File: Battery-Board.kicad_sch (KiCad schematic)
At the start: 0 parts

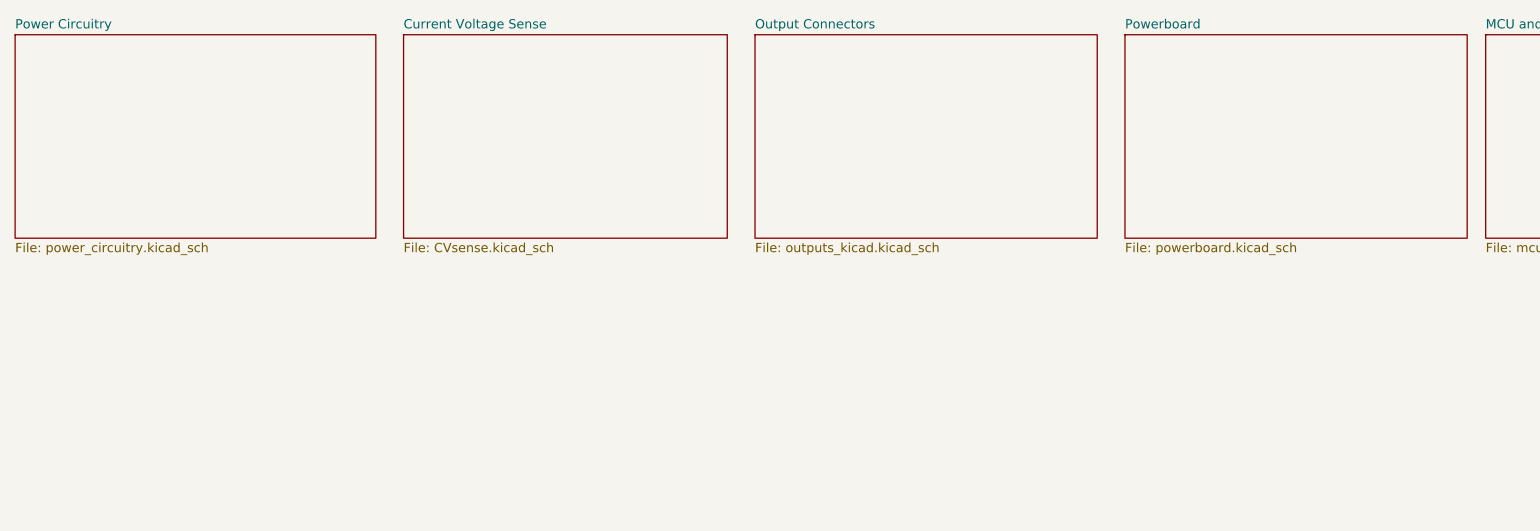
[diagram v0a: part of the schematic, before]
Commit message: started sorting and cleaning up schemativc
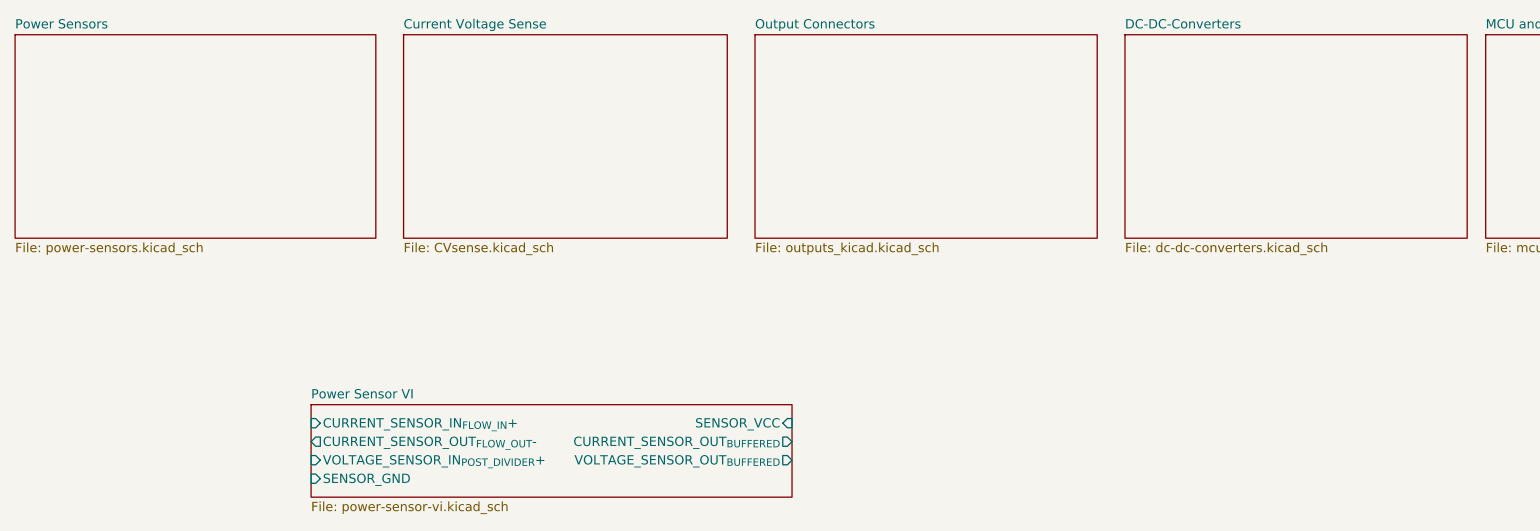
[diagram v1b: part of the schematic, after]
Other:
- sheet Power Circuitry renamed Power Sensors
- sheet Powerboard renamed DC-DC-Converters
- added sheet Power Sensor VI (power-sensor-vi.kicad_sch)
- sheet DC-DC-Converters: file powerboard.kicad_sch -> dc-dc-converters.kicad_sch
- sheet Power Sensors: file power_circuitry.kicad_sch -> power-sensors.kicad_sch
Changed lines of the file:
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@@
 			(color 0 0 0 0.0000)
 		)
-		(property "Sheetname" "Powerboard"
+		(property "Sheetname" "DC-DC-Converters"
 			(at 167.64 14.5284 0)
 			(effects
@@
 			)
 		)
-		(property "Sheetfile" "powerboard.kicad_sch"
+		(property "Sheetfile" "dc-dc-converters.kicad_sch"
 			(at 167.64 43.7646 0)
 			(effects
@@
 	)
 	(sheet
+		(at 55.88 66.04)
+		(size 66.04 12.7)
+		(fields_autoplaced yes)
+		(stroke
+			(width 0.1524)
+			(type solid)
+		)
+		(fill
+			(color 255 255 194 1.0000)
+		)
+		(property "Sheetname" "Power Sensor VI"
+			(at 55.88 65.3284 0)
+			(effects
+				(font
+					(size 1.27 1.27)
+				)
+				(justify left bottom)
+			)
+		)
+		(property "Sheetfile" "power-sensor-vi.kicad_sch"
+			(at 55.88 79.3246 0)
+			(effects
+				(font
+					(size 1.27 1.27)
+				)
+				(justify left top)
+			)
+		)
+		(pin "CURRENT_SENSOR_IN_{FLOW_IN}+" input
+			(at 55.88 68.58 180)
+			(effects
+				(font
+					(size 1.27 1.27)
+				)
+				(justify left)
+			)
+		)
+		(pin "SENSOR_VCC" input
+			(at 121.92 68.58 0)
+			(effects
+				(font
+					(size 1.27 1.27)
+				)
+				(justify right)
+			)
+		)
+		(pin "CURRENT_SENSOR_OUT_{FLOW_OUT}-" output
+			(at 55.88 71.12 180)
+			(effects
+				(font
+					(size 1.27 1.27)
+				)
+				(justify left)
+			)
+		)
+		(pin "CURRENT_SENSOR_OUT_{BUFFERED}" output
+			(at 121.92 71.12 0)
+			(effects
+				(font
+					(size 1.27 1.27)
+				)
+				(justify right)
+			)
+		)
+		(pin "SENSOR_GND" input
+			(at 55.88 76.2 180)
+			(effects
+				(font
+					(size 1.27 1.27)
+				)
+				(justify left)
+			)
+		)
+		(pin "VOLTAGE_SENSOR_IN_{POST_DIVIDER}+" input
+			(at 55.88 73.66 180)
+			(effects
+				(font
+					(size 1.27 1.27)
+				)
+				(justify left)
+			)
+		)
+		(pin "VOLTAGE_SENSOR_OUT_{BUFFERED}" output
+			(at 121.92 73.66 0)
+			(effects
+				(font
+					(size 1.27 1.27)
+				)
+				(justify right)
+			)
+		)
+		(instances
+			(project "Battery-Board"
+				(path "/7996c6a7-339e-40c9-8e7c-4c4bf8c43339"
+					(page "7")
+				)
+			)
+		)
+	)
+	(sheet
 		(at 217.17 15.24)
 		(size 52.07 27.94)
@@
 			(color 0 0 0 0.0000)
 		)
-		(property "Sheetname" "Power Circuitry"
+		(property "Sheetname" "Power Sensors"
 			(at 15.24 14.5284 0)
 			(effects
@@
 			)
 		)
-		(property "Sheetfile" "power_circuitry.kicad_sch"
+		(property "Sheetfile" "power-sensors.kicad_sch"
 			(at 15.24 43.7646 0)
 			(effects

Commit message: Started Layout and cleaned up schematic
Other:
- removed sheet Current Voltage Sense
- removed sheet Output Connectors
- removed sheet Power Sensors
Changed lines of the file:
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@@
-	)
-	(sheet
-		(at 116.84 15.24)
-		(size 46.99 27.94)
-		(fields_autoplaced yes)
-		(stroke
-			(width 0.1524)
-			(type solid)
-		)
-		(fill
-			(color 0 0 0 0.0000)
-		)
-		(property "Sheetname" "Output Connectors"
-			(at 116.84 14.5284 0)
-			(effects
-				(font
-					(size 1.27 1.27)
-				)
-				(justify left bottom)
-			)
-		)
-		(property "Sheetfile" "outputs_kicad.kicad_sch"
-			(at 116.84 43.7646 0)
-			(effects
-				(font
-					(size 1.27 1.27)
-				)
-				(justify left top)
-			)
-		)
-		(instances
-			(project "Battery-Board"
-				(path "/7996c6a7-339e-40c9-8e7c-4c4bf8c43339"
-					(page "4")
-				)
-			)
-		)
 	)
 	(sheet
@@
 				)
 			)
-		)
-	)
-	(sheet
-		(at 15.24 15.24)
-		(size 49.53 27.94)
-		(fields_autoplaced yes)
-		(stroke
-			(width 0.1524)
-			(type solid)
-		)
-		(fill
-			(color 0 0 0 0.0000)
-		)
-		(property "Sheetname" "Power Sensors"
-			(at 15.24 14.5284 0)
-			(effects
-				(font
-					(size 1.27 1.27)
-				)
-				(justify left bottom)
-			)
-		)
-		(property "Sheetfile" "power-sensors.kicad_sch"
-			(at 15.24 43.7646 0)
-			(effects
-				(font
-					(size 1.27 1.27)
-				)
-				(justify left top)
-			)
-		)
-		(instances
-			(project "Battery-Board"
-				(path "/7996c6a7-339e-40c9-8e7c-4c4bf8c43339"
-					(page "2")
-				)
-			)
-		)
-	)
-	(sheet
-		(at 68.58 15.24)
-		(size 44.45 27.94)
-		(fields_autoplaced yes)
-		(stroke
-			(width 0.1524)
-			(type solid)
-		)
-		(fill
-			(color 0 0 0 0.0000)
-		)
-		(property "Sheetname" "Current Voltage Sense"
-			(at 68.58 14.5284 0)
-			(effects
-				(font
-					(size 1.27 1.27)
-				)
-				(justify left bottom)
-			)
-		)
-		(property "Sheetfile" "CVsense.kicad_sch"
-			(at 68.58 43.7646 0)
-			(effects
-				(font
-					(size 1.27 1.27)
-				)
-				(justify left top)
-			)
-		)
-		(instances
-			(project "Battery-Board"
-				(path "/7996c6a7-339e-40c9-8e7c-4c4bf8c43339"
-					(page "6")
-				)
-			)

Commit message: A
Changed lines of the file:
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@@
 	(paper "A4")
 	(sheet
-		(at 167.64 15.24)
+		(at 46.99 27.94)
 		(size 46.99 27.94)
 		(fields_autoplaced yes)
@@
 		)
 		(property "Sheetname" "DC-DC-Converters"
-			(at 167.64 14.5284 0)
+			(at 46.99 27.2284 0)
 			(effects
 				(font
@@
 		)
 		(property "Sheetfile" "dc-dc-converters.kicad_sch"
-			(at 167.64 43.7646 0)
+			(at 46.99 56.4646 0)
 			(effects
 				(font
@@
 	)
 	(sheet
-		(at 217.17 15.24)
+		(at 96.52 27.94)
 		(size 52.07 27.94)
 		(fields_autoplaced yes)
@@
 		)
 		(property "Sheetname" "MCU and sensors"
-			(at 217.17 14.5284 0)
+			(at 96.52 27.2284 0)
 			(effects
 				(font
@@
 		)
 		(property "Sheetfile" "mcu.kicad_sch"
-			(at 217.17 43.7646 0)
+			(at 96.52 56.4646 0)
 			(effects
 				(font

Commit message: A
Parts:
- added C52, C53, C87, C88: 10u, Capacitor_SMD:C_0805_2012Metric, symbol Device:C
- added C54, C86, C89: 100u, Capacitor_SMD:CP_Elec_6.3x9.9, symbol Device:C_Polarized
- added D11, D12, D13: BLUE, LED_SMD:LED_0603_1608Metric, symbol Device:LED
- added J6: Female Conn, ecocad_lib_footprints:DB7W2-Female, symbol ecocad_lib_symbols:DB7W2-Female
- added J7: BATT IN, ecocad_lib_footprints:PHOENIX_1017521, symbol ecocad_lib_symbols:PHNX_CONN_1017521
- added JP3: 12V Buck, symbol Jumper:Jumper_2_Open
- added JP4: 24V, symbol Jumper:Jumper_2_Open
- added JP5: 7V Buck, symbol Jumper:Jumper_2_Open
- added R43, R44, R45: 1k, Resistor_SMD:R_0603_1608Metric, symbol Device:R
- added U17: AZ1084-3.3, Package_TO_SOT_SMD:TO-252-2, symbol Regulator_Linear:AZ1084-3.3
- added U4: AZ1084-5.0, Package_TO_SOT_SMD:TO-252-2, symbol Regulator_Linear:AZ1084-5.0
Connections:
- new net: D12.2 (A), R44.2
- new net: C52.1, JP3.1 (A), JP4.1 (A), JP5.1 (A), U4.3 (VI)
- new net: D11.2 (A), R43.2
- new net: D13.2 (A), R45.2
- new net +3V3: C88.1, C89.1, R44.1, U17.2 (VO)
- new net +5V: C53.1, C54.1, C86.1, C87.1, R43.1, U17.3 (VI), U4.2 (VO)
- new net CANH: J6.2
- new net CANL: J6.5
- new net GND: C52.2, C53.2, C54.2, C86.2, C87.2, C88.2, C89.2, D11.1 (K), D12.1 (K), D13.1 (K), J6.9, J7.1, U17.1 (GND), U4.1 (GND)
- new net IN_{24V}: J7.2, JP4.2 (B), R45.1
- new net OUT_{12V}: J6.1, J6.3, J6.4, JP3.2 (B)
- new net OUT_{7V}: J6.8, JP5.2 (B)
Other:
- removed sheet Power Sensor VI
- sheet DC-DC-Converters ports: added IMON_{12V}, IMON_{7V}, IMON_{IN}, IN_{24V}, OUT_{12V}, OUT_{7V}, PG_{12V}, PG_{7V}, VMON_{12V}, VMON_{7V}, VMON_{IN}; removed none
- sheet MCU and sensors ports: added CANH, CANL, IMON_{12V}, IMON_{7V}, IMON_{IN}, PG_{12V}, PG_{7V}, VMON_{12V}, VMON_{7V}, VMON_{IN}; removed none
- company: (none) -> University of Alberta EcoCar Team
- title: (none) -> Battery Power Board

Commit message: A
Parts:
- R43, R44, R45: footprint Resistor_SMD:R_0603_1608Metric -> Resistor_SMD:R_0805_2012Metric
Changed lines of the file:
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@@
 	(label "OUT_{12V}"
 		(at 111.76 96.52 0)
+		(fields_autoplaced yes)
 		(effects
 			(font
@@
 	(label "CANL"
 		(at 165.1 109.22 270)
+		(fields_autoplaced yes)
 		(effects
 			(font
@@
 	(label "IN_{24V}"
 		(at 57.15 83.82 180)
+		(fields_autoplaced yes)
 		(effects
 			(font
@@
 	(label "CANH"
 		(at 162.56 109.22 270)
+		(fields_autoplaced yes)
 		(effects
 			(font
@@
 	(label "OUT_{7V}"
 		(at 111.76 81.28 0)
+		(fields_autoplaced yes)
 		(effects
 			(font
@@
 			)
 		)
-		(property "Footprint" "Resistor_SMD:R_0603_1608Metric"
+		(property "Footprint" "Resistor_SMD:R_0805_2012Metric"
 			(at 155.702 163.83 90)
 			(effects
@@
 			)
 		)
-		(property "Footprint" "Resistor_SMD:R_0603_1608Metric"
+		(property "Footprint" "Resistor_SMD:R_0805_2012Metric"
 			(at 89.662 163.83 90)
 			(effects
@@
 			)
 		)
-		(property "Footprint" "Resistor_SMD:R_0603_1608Metric"
+		(property "Footprint" "Resistor_SMD:R_0805_2012Metric"
 			(at 49.022 95.25 90)
 			(effects

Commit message: Done
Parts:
- removed C86: 100u, Capacitor_SMD:CP_Elec_6.3x9.9, symbol Device:C_Polarized
- removed JP4: 24V, symbol Jumper:Jumper_2_Open
- removed U17: AZ1084-3.3, Package_TO_SOT_SMD:TO-252-2, symbol Regulator_Linear:AZ1084-3.3
- removed U4: AZ1084-5.0, Package_TO_SOT_SMD:TO-252-2, symbol Regulator_Linear:AZ1084-5.0
- added C86: 10u, Capacitor_SMD:C_0805_2012Metric, symbol Device:C
- added C94: 100n, Capacitor_SMD:C_0603_1608Metric, symbol Device:C
- added C95: 2n2, Capacitor_SMD:C_0603_1608Metric, symbol Device:C
- added D18, D19: BLUE, LED_SMD:LED_0603_1608Metric, symbol Device:LED
- added R48: 2k, Resistor_SMD:R_0603_1608Metric, symbol Device:R
- added R49: 511k, Resistor_SMD:R_0603_1608Metric, symbol Device:R
- added R50: 23k7, Resistor_SMD:R_0603_1608Metric, symbol Device:R
- added R51: 47k, Resistor_SMD:R_0603_1608Metric, symbol Device:R
- added R52: 1k, Resistor_SMD:R_0603_1608Metric, symbol Device:R
- added R53: 620R, Resistor_SMD:R_0603_1608Metric, symbol Device:R
- added U18: TPS2596, Package_SO:TI_SO-PowerPAD-8, symbol H2_Parts:TPS2596
- added U19, U20: AZ1117-5.0, Package_TO_SOT_SMD:SOT-223-3_TabPin2, symbol Regulator_Linear:AZ1117-5.0
- added U4: AZ1117IH-3.3, Package_TO_SOT_SMD:SOT-223-3_TabPin2, symbol ecocad_lib_symbols:AZ1117IH-3.3
- JP3, JP5: footprint (none) -> ecocad_lib_footprints:J_0603_Triangular
- R43, R44, R45: footprint Resistor_SMD:R_0805_2012Metric -> Resistor_SMD:R_0603_1608Metric
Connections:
- net +3V3: now also U4.2 (VO)
- net +5V: now also C86.1, R52.1, U19.2 (VO), U20.2 (VO), U4.3 (VI)
- net GND: now also J7.2, C86.2, C94.2, C95.2, D18.1 (K), D19.1 (K), R51.2, R53.2, U18.1 (GND), U18.9 (PAD), U19.1 (GND), U20.1 (GND), U4.1 (GND); no longer J7.1
- net IN_{24V}: now also J7.1; no longer J7.2
- net at JP3.1 (A), JP5.1 (A): now also C94.1, R48.1, R49.2, U18.4 (IN); no longer C52.1
- new net: C52.1, U18.5 (OUT), U19.3 (VI), U20.3 (VI)
- new net: D19.2 (A), R52.2
- new net: R49.1, R50.1, U18.3 (EN/UVLO)
- new net: C95.1, U18.2 (dV/dT)
- new net: R50.2, R51.1, U18.8 (OVLO)
- new net: D18.2 (A), R48.2
- new net I_{MON}: R53.1, U18.7 (ILM)
- new net ~{FAULT}: U18.6 (~{FAULT})
- no-connect marks 0 -> 1
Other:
- note added: "1% tolerance"
- note added: "TPS25963 eFuse 2A 12V"
- moved on the sheet: C52, C53, C54, C87, C88, C89, D11, D12, D13, J6, J7, JP3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
